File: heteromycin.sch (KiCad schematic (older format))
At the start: 0 parts

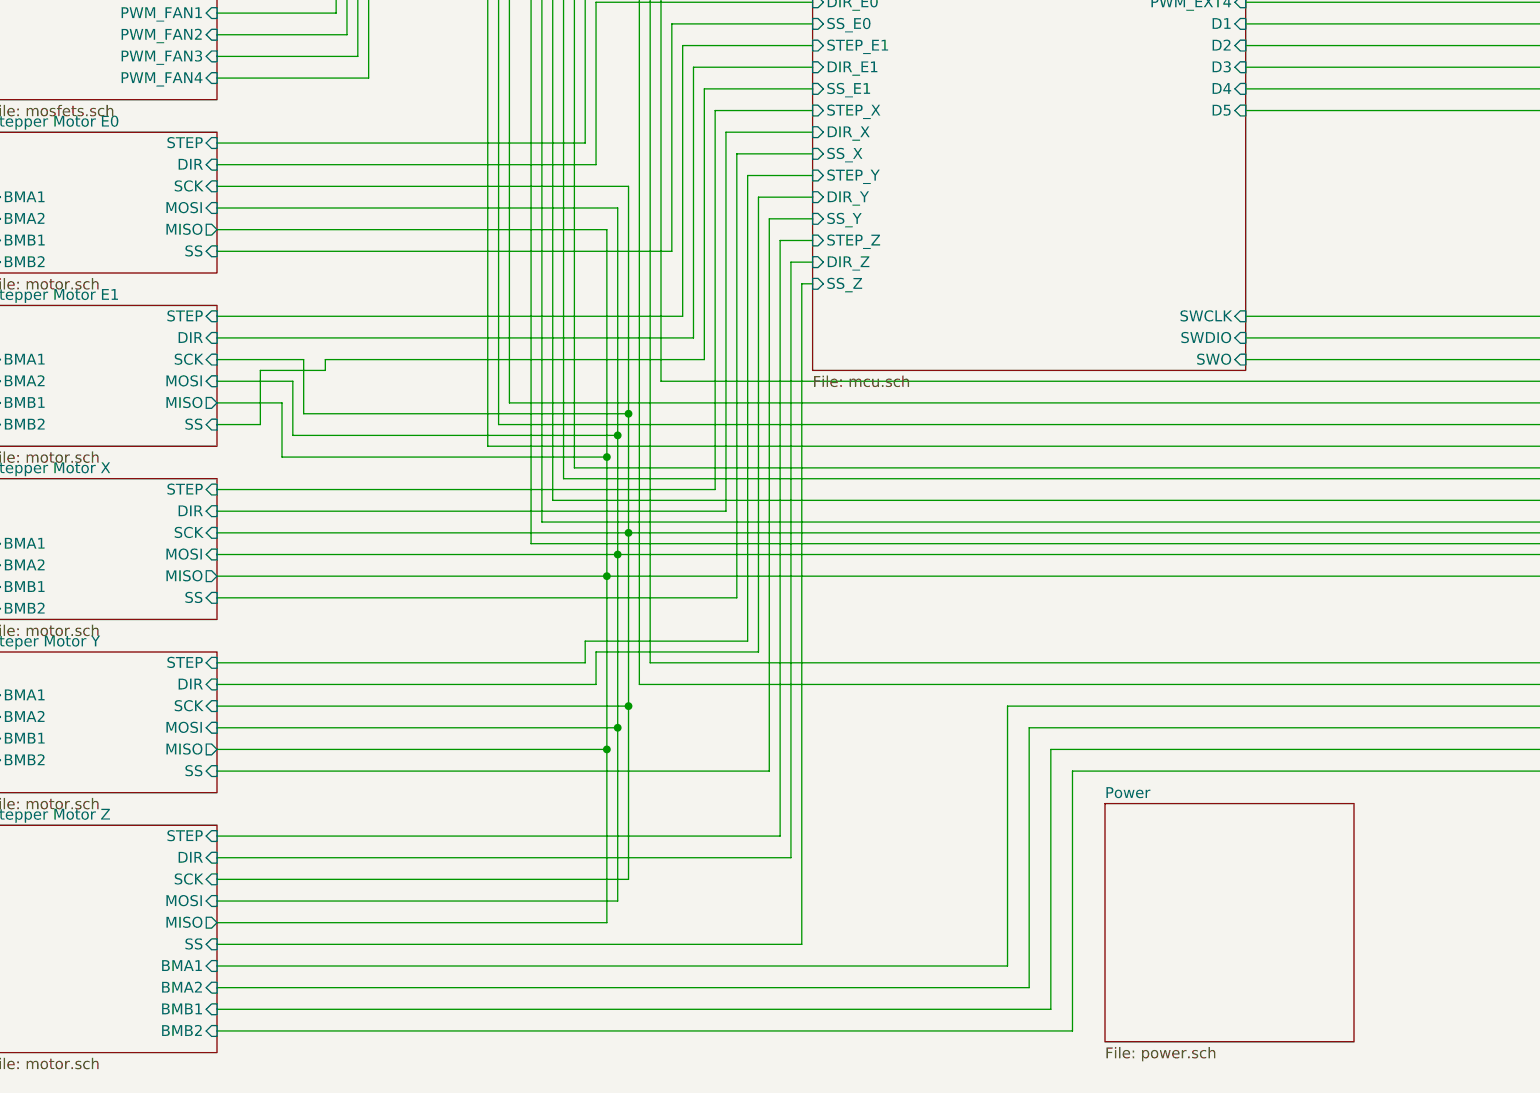
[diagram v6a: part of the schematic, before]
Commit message: Connected TMC DIAG pins to MCU
We had some pins free, so I decided to connect them, so that we
don't need to use the ENDSTOP OVER SPI feature.
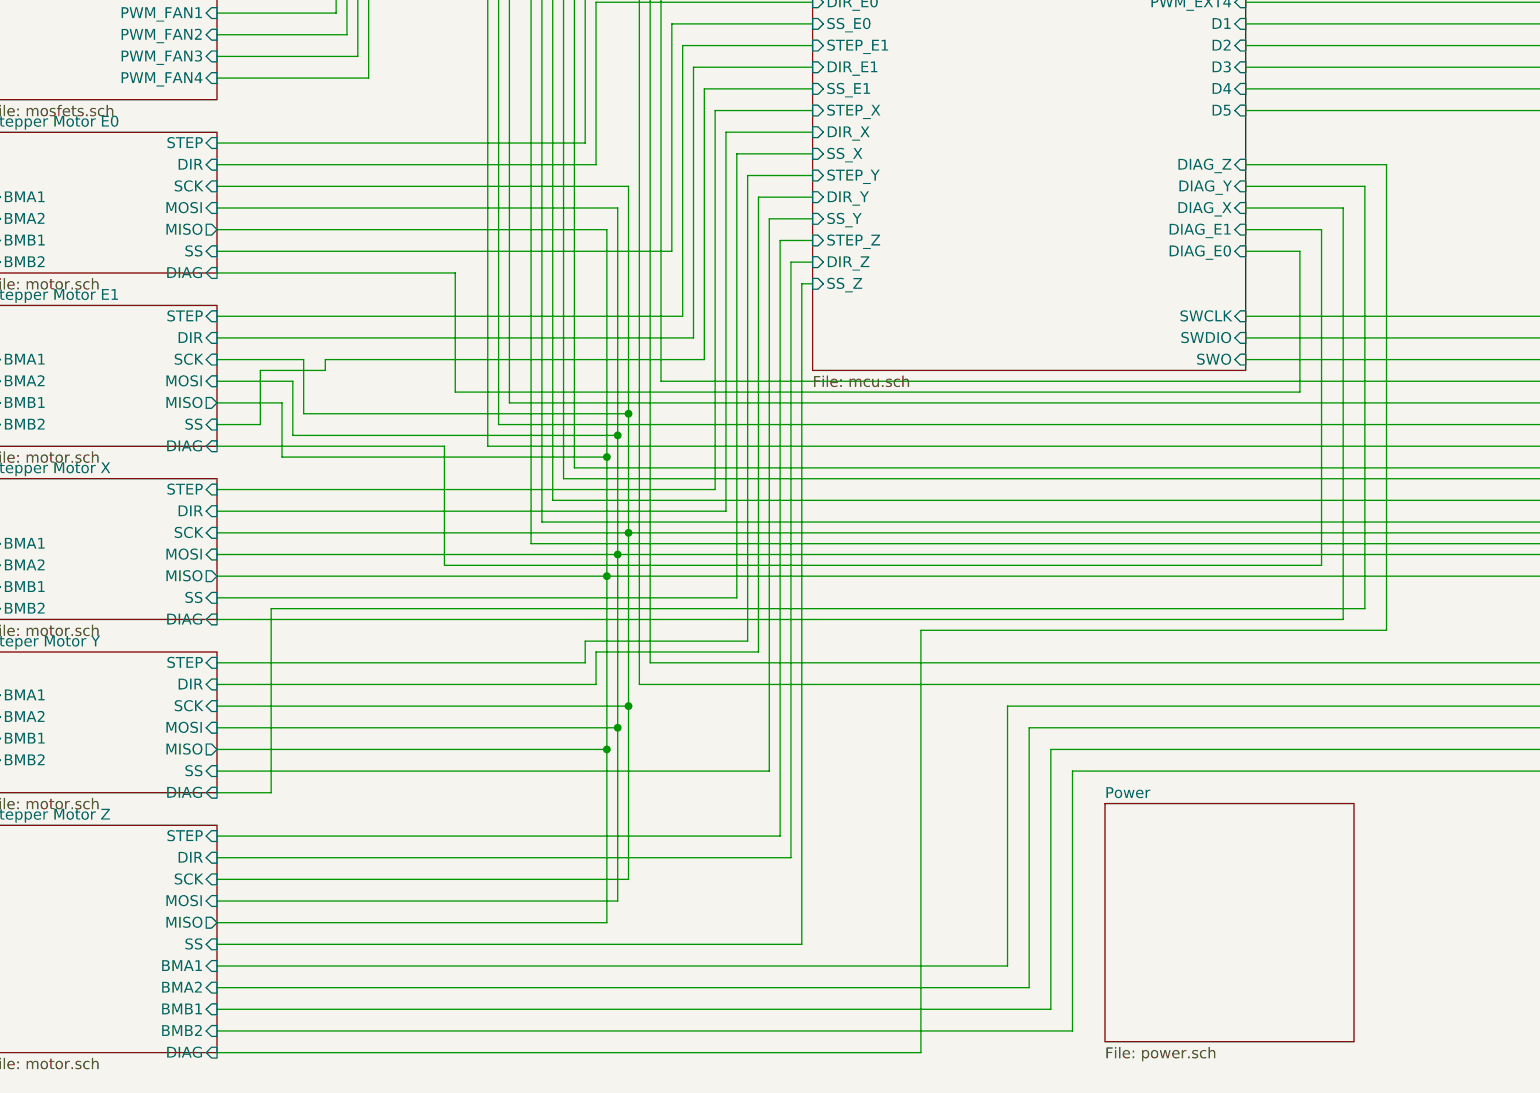
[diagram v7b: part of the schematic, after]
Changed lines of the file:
@@
 F58 "D4" I R 6350 3250 50
 F59 "D5" I R 6350 3350 50
+F60 "DIAG_Z" I R 6350 3600 50
+F61 "DIAG_Y" I R 6350 3700 50
+F62 "DIAG_X" I R 6350 3800 50
+F63 "DIAG_E1" I R 6350 3900 50
+F64 "DIAG_E0" I R 6350 4000 50
 $EndSheet
 $Sheet
@@
 F10 "BMB2" I L 550 5650 50
 F11 "BMB1" I L 550 5550 50
+F12 "DIAG" I R 1600 5700 50
 $EndSheet
 $Sheet
@@
 F10 "BMB2" I L 550 6350 50
 F11 "BMB1" I L 550 6250 50
+F12 "DIAG" I R 1600 6500 50
 $EndSheet
 $Sheet
@@
 F10 "BMB1" I R 1600 7500 50
 F11 "SS" I R 1600 7200 50
+F12 "DIAG" I R 1600 7700 50
 $EndSheet
 $Sheet
@@
 F10 "BMB2" I L 550 4050 50
 F11 "BMB1" I L 550 3950 50
+F12 "DIAG" I R 1600 4100 50
 $EndSheet
 $Sheet
@@
 F10 "BMB2" I L 550 4800 50
 F11 "BMB1" I L 550 4700 50
+F12 "DIAG" I R 1600 4900 50
 $EndSheet
 $Sheet
@@
 Wire Wire Line
 	2300 2450 4350 2450
+Wire Wire Line
+	6350 4000 6600 4000
+Wire Wire Line
+	6600 4000 6600 4650
+Wire Wire Line
+	6600 4650 2700 4650
+Wire Wire Line
+	2700 4650 2700 4100
+Wire Wire Line
+	2700 4100 1600 4100
+Wire Wire Line
+	1600 4900 2650 4900
+Wire Wire Line
+	2650 4900 2650 5450
+Wire Wire Line
+	2650 5450 6700 5450
+Wire Wire Line
+	6700 5450 6700 3900
+Wire Wire Line
+	6700 3900 6350 3900
+Wire Wire Line
+	1600 5700 6800 5700
+Wire Wire Line
+	6800 5700 6800 3800
+Wire Wire Line
+	6800 3800 6350 3800
+Wire Wire Line
+	6350 3700 6900 3700
+Wire Wire Line
+	6900 3700 6900 5650
+Wire Wire Line
+	6900 5650 1850 5650
+Wire Wire Line
+	1850 5650 1850 6500
+Wire Wire Line
+	1850 6500 1600 6500
+Wire Wire Line
+	1600 7700 4850 7700
+Wire Wire Line
+	4850 7700 4850 5750
+Wire Wire Line
+	4850 5750 7000 5750
+Wire Wire Line
+	7000 5750 7000 3600
+Wire Wire Line
+	7000 3600 6350 3600
 $EndSCHEMATC
